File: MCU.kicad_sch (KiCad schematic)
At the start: 0 parts

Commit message: add power and processor and connectors
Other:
- note added: "Add programming connectors in this sheet"
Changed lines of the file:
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@@
 (kicad_sch (version 20211123) (generator eeschema)
   (paper "A4")
+  (text "Add programming connectors in this sheet \n" (at 17.78 19.05 0)
+    (effects (font (size 0.762 0.762)) (justify left bottom))
+  )
 )

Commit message: MCU added
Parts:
- added ?: STM32H725ZGT6, symbol STM32H725ZGT6:STM32H725ZGT6
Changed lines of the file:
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@@
     (effects (font (size 0.762 0.762)) (justify left bottom))
   )
+  (symbol (lib_id "STM32H725ZGT6:STM32H725ZGT6") (at 80.645 46.99 0) (unit 1)
+    (in_bom yes) (on_board yes) (fields_autoplaced)
+    (property "Reference" "?" (id 0) (at 189.23 35.3312 0))
+    (property "Value" "STM32H725ZGT6" (id 1) (at 189.23 37.8712 0))
+    (property "Footprint" "" (id 2) (at 80.645 46.99 0)
+      (effects (font (size 1.27 1.27)) hide)
+    )
+    (property "Datasheet" "" (id 3) (at 80.645 46.99 0)
+      (effects (font (size 1.27 1.27)) hide)
+    )
+    (property "Reference_1" "IC" (id 4) (at 189.23 40.4112 0))
+    (property "Value_1" "STM32H725ZGT6" (id 5) (at 189.23 42.9512 0))
+    (property "Footprint_1" "QFP50P2200X2200X160-144N" (id 6) (at 180.975 129.21 0)
+      (effects (font (size 1.27 1.27)) (justify left top) hide)
+    )
+    (property "Datasheet_1" "https://www.st.com/resource/en/datasheet/stm32h725ag.pdf" (id 7) (at 180.975 229.21 0)
+      (effects (font (size 1.27 1.27)) (justify left top) hide)
+    )
+    (property "Height" "1.6" (id 8) (at 180.975 429.21 0)
+      (effects (font (size 1.27 1.27)) (justify left top) hide)
+    )
+    (property "Mouser Part Number" "511-STM32H725ZGT6" (id 9) (at 180.975 529.21 0)
+      (effects (font (size 1.27 1.27)) (justify left top) hide)
+    )
+    (property "Mouser Price/Stock" "https://www.mouser.co.uk/ProductDetail/STMicroelectronics/STM32H725ZGT6?qs=sPbYRqrBIVkxUSEHgllpOw%3D%3D" (id 10) (at 180.975 629.21 0)
+      (effects (font (size 1.27 1.27)) (justify left top) hide)
+    )
+    (property "Manufacturer_Name" "STMicroelectronics" (id 11) (at 180.975 729.21 0)
+      (effects (font (size 1.27 1.27)) (justify left top) hide)
+    )
+    (property "Manufacturer_Part_Number" "STM32H725ZGT6" (id 12) (at 180.975 829.21 0)
+      (effects (font (size 1.27 1.27)) (justify left top) hide)
+    )
+    (pin "1")
+    (pin "10")
+    (pin "100")
+    (pin "101")
+    (pin "102")
+    (pin "103")
+    (pin "104")
+    (pin "105")
+    (pin "106")
+    (pin "107")
+    (pin "108")
+    (pin "109")
+    (pin "11")
+    (pin "110")
+    (pin "111")
+    (pin "112")
+    (pin "113")
+    (pin "114")
+    (pin "115")
+    (pin "116")
+    (pin "117")
+    (pin "118")
+    (pin "119")
+    (pin "12")
+    (pin "120")
+    (pin "121")
+    (pin "122")
+    (pin "123")
+    (pin "124")
+    (pin "125")
+    (pin "126")
+    (pin "127")
+    (pin "128")
+    (pin "129")
+    (pin "13")
+    (pin "130")
+    (pin "131")
+    (pin "132")
+    (pin "133")
+    (pin "134")
+    (pin "135")
+    (pin "136")
+    (pin "137")
+    (pin "138")
+    (pin "139")
+    (pin "14")
+    (pin "140")
+    (pin "141")
+    (pin "142")
+    (pin "143")
+    (pin "144")
+    (pin "15")
+    (pin "16")
+    (pin "17")
+    (pin "18")
+    (pin "19")
+    (pin "2")
+    (pin "20")
+    (pin "21")
+    (pin "22")
+    (pin "23")
+    (pin "24")
+    (pin "25")
+    (pin "26")
+    (pin "27")
+    (pin "28")
+    (pin "29")
+    (pin "3")
+    (pin "30")
+    (pin "31")
+    (pin "32")
+    (pin "33")
+    (pin "34")
+    (pin "35")
+    (pin "36")
+    (pin "37")
+    (pin "38")
+    (pin "39")
+    (pin "4")
+    (pin "40")
+    (pin "41")
+    (pin "42")
+    (pin "43")
+    (pin "44")
+    (pin "45")
+    (pin "46")
+    (pin "47")
+    (pin "48")
+    (pin "49")
+    (pin "5")
+    (pin "50")
+    (pin "51")
+    (pin "52")
+    (pin "53")
+    (pin "54")
+    (pin "55")
+    (pin "56")
+    (pin "57")
+    (pin "58")
+    (pin "59")
+    (pin "6")
+    (pin "60")
+    (pin "61")
+    (pin "62")
+    (pin "63")
+    (pin "64")
+    (pin "65")
+    (pin "66")
+    (pin "67")
+    (pin "68")
+    (pin "69")
+    (pin "7")
+    (pin "70")
+    (pin "71")
+    (pin "72")
+    (pin "73")
+    (pin "74")
+    (pin "75")
+    (pin "76")
+    (pin "77")
+    (pin "78")
+    (pin "79")
+    (pin "8")
+    (pin "80")
+    (pin "81")
+    (pin "82")
+    (pin "83")
+    (pin "84")
+    (pin "85")
+    (pin "86")
+    (pin "87")
+    (pin "88")
+    (pin "89")
+    (pin "9")
+    (pin "90")
+    (pin "91")
+    (pin "92")
+    (pin "93")
+    (pin "94")
+    (pin "95")
+    (pin "96")
+    (pin "97")
+    (pin "98")
+    (pin "99")
+  )
 )

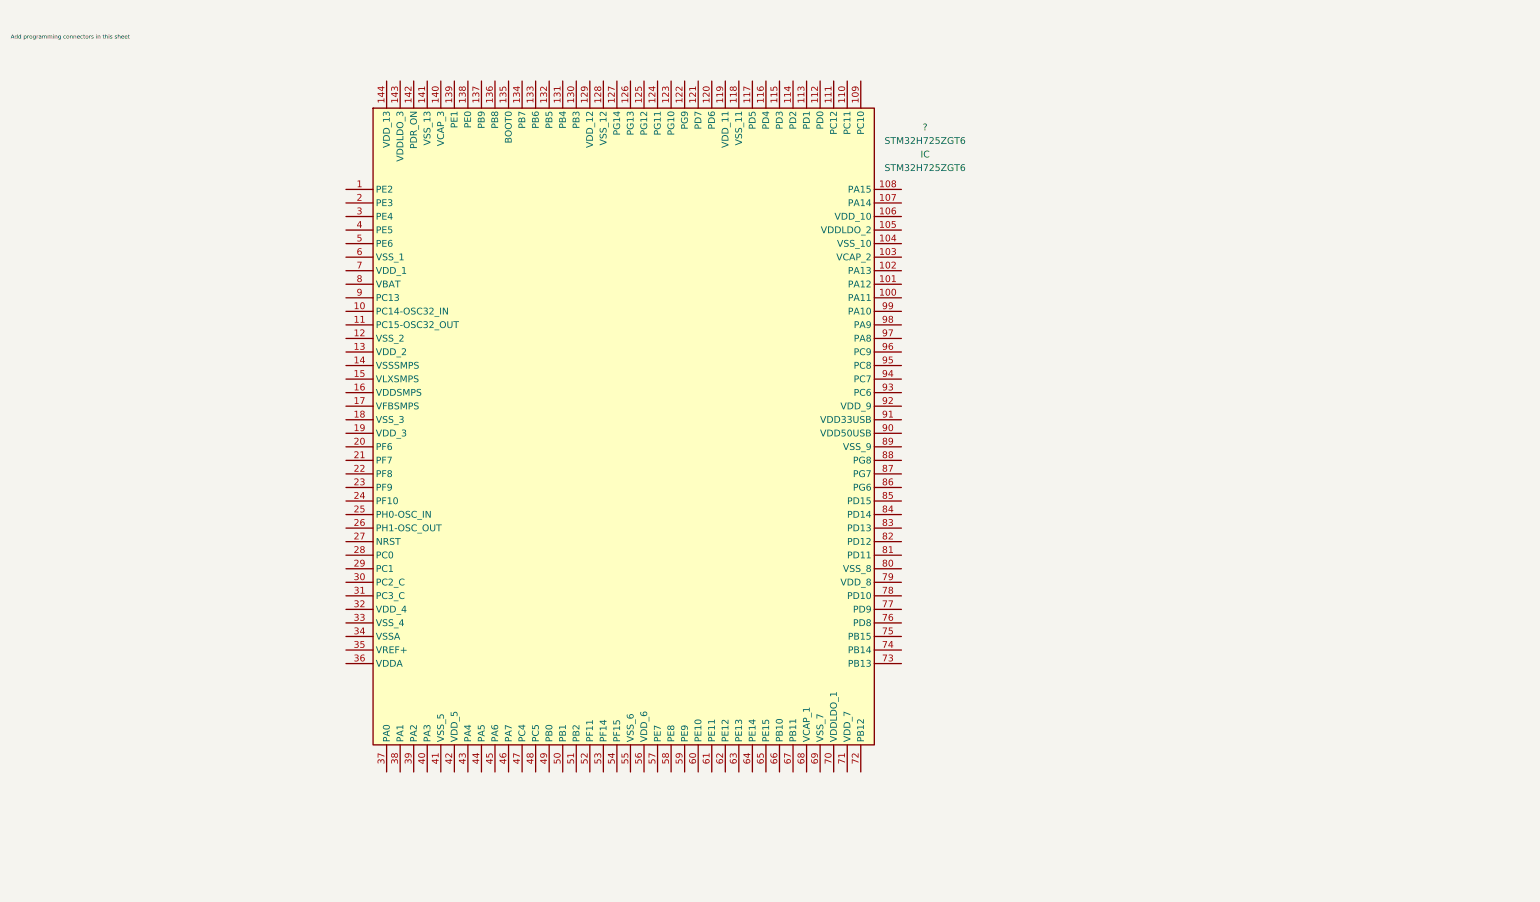
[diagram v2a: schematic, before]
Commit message: MCU_pinout_except_timer please add connector symbols and footprint folder, i will send you parts throughout the day
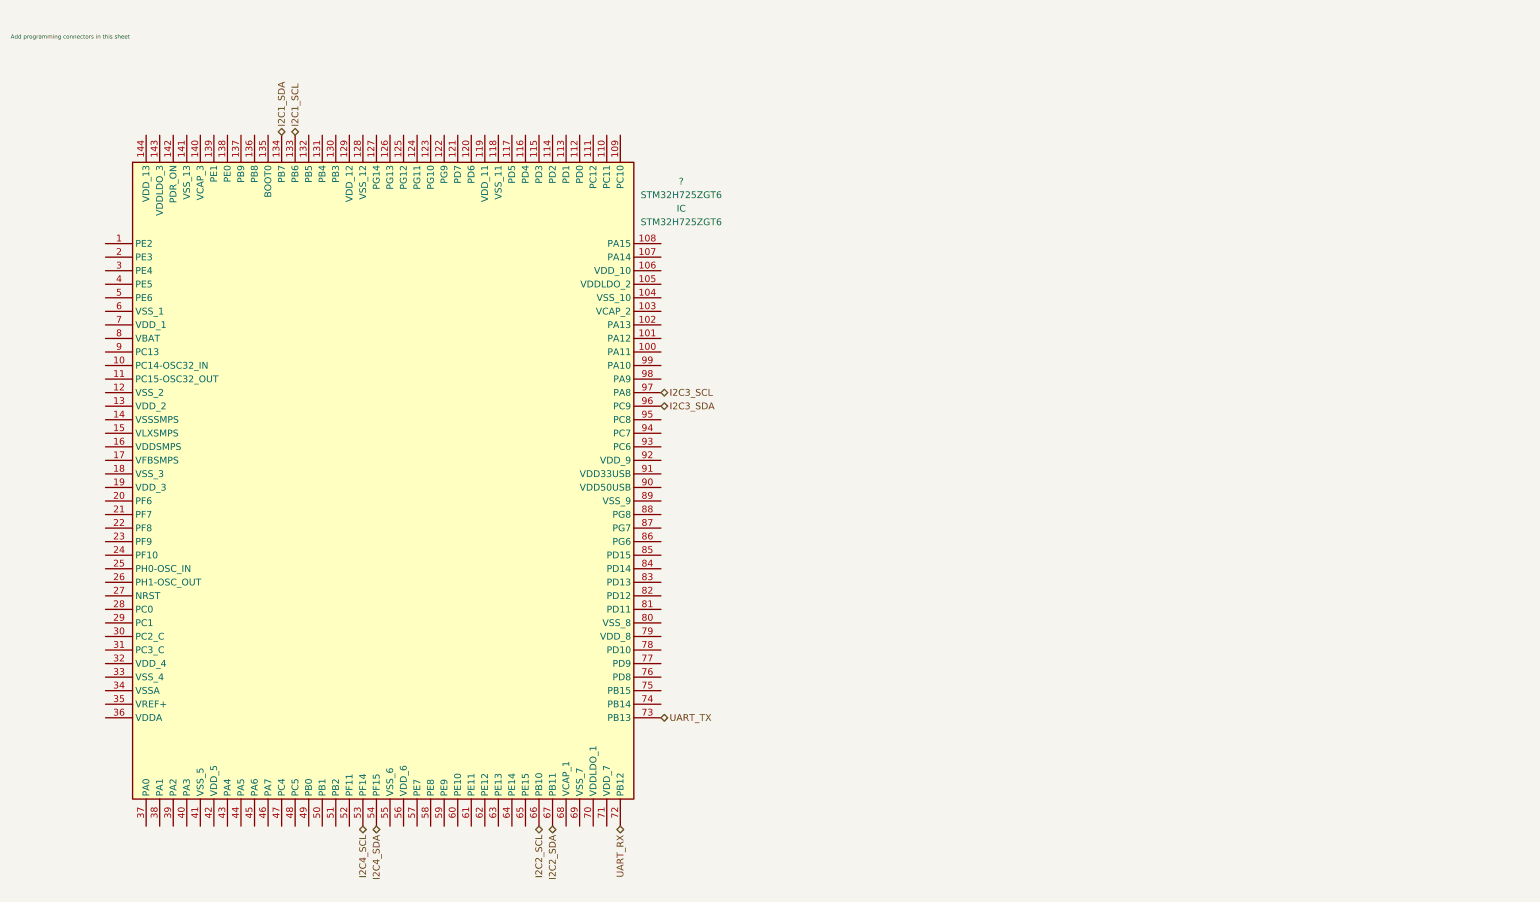
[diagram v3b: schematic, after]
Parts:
- removed ?: STM32H725ZGT6, symbol STM32H725ZGT6:STM32H725ZGT6
- added ?: STM32H725ZGT6, symbol STM32H725ZGT6:STM32H725ZGT6
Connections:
- new net I2C1_SCL: ?.133 (PB6)
- new net I2C1_SDA: ?.134 (PB7)
- new net I2C2_SCL: ?.66 (PB10)
- new net I2C2_SDA: ?.67 (PB11)
- new net I2C3_SCL: ?.97 (PA8)
- new net I2C3_SDA: ?.96 (PC9)
- new net I2C4_SCL: ?.53 (PF14)
- new net I2C4_SDA: ?.54 (PF15)
- new net UART_RX: ?.72 (PB12)
- new net UART_TX: ?.73 (PB13)
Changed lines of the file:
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@@
     (effects (font (size 0.762 0.762)) (justify left bottom))
   )
-  (symbol (lib_id "STM32H725ZGT6:STM32H725ZGT6") (at 80.645 46.99 0) (unit 1)
+  (hierarchical_label "I2C4_SDA" (shape bidirectional) (at 86.36 166.37 270)
+    (effects (font (size 1.27 1.27)) (justify right))
+  )
+  (hierarchical_label "I2C2_SCL" (shape bidirectional) (at 116.84 166.37 270)
+    (effects (font (size 1.27 1.27)) (justify right))
+  )
+  (hierarchical_label "I2C4_SCL" (shape bidirectional) (at 83.82 166.37 270)
+    (effects (font (size 1.27 1.27)) (justify right))
+  )
+  (hierarchical_label "UART_RX" (shape bidirectional) (at 132.08 166.37 270)
+    (effects (font (size 1.27 1.27)) (justify right))
+  )
+  (hierarchical_label "I2C2_SDA" (shape bidirectional) (at 119.38 166.37 270)
+    (effects (font (size 1.27 1.27)) (justify right))
+  )
+  (hierarchical_label "UART_TX" (shape bidirectional) (at 139.7 146.05 0)
+    (effects (font (size 1.27 1.27)) (justify left))
+  )
+  (hierarchical_label "I2C1_SCL" (shape bidirectional) (at 71.12 36.83 90)
+    (effects (font (size 1.27 1.27)) (justify left))
+  )
+  (hierarchical_label "I2C3_SCL" (shape bidirectional) (at 139.7 85.09 0)
+    (effects (font (size 1.27 1.27)) (justify left))
+  )
+  (hierarchical_label "I2C1_SDA" (shape bidirectional) (at 68.58 36.83 90)
+    (effects (font (size 1.27 1.27)) (justify left))
+  )
+  (hierarchical_label "I2C3_SDA" (shape bidirectional) (at 139.7 87.63 0)
+    (effects (font (size 1.27 1.27)) (justify left))
+  )
+  (symbol (lib_id "STM32H725ZGT6:STM32H725ZGT6") (at 35.56 57.15 0) (unit 1)
     (in_bom yes) (on_board yes) (fields_autoplaced)
-    (property "Reference" "?" (id 0) (at 189.23 35.3312 0))
-    (property "Value" "STM32H725ZGT6" (id 1) (at 189.23 37.8712 0))
-    (property "Footprint" "" (id 2) (at 80.645 46.99 0)
+    (property "Reference" "?" (id 0) (at 143.51 45.4912 0))
+    (property "Value" "STM32H725ZGT6" (id 1) (at 143.51 48.0312 0))
+    (property "Footprint" "" (id 2) (at 35.56 57.15 0)
       (effects (font (size 1.27 1.27)) hide)
     )
-    (property "Datasheet" "" (id 3) (at 80.645 46.99 0)
+    (property "Datasheet" "" (id 3) (at 35.56 57.15 0)
       (effects (font (size 1.27 1.27)) hide)
     )
-    (property "Reference_1" "IC" (id 4) (at 189.23 40.4112 0))
-    (property "Value_1" "STM32H725ZGT6" (id 5) (at 189.23 42.9512 0))
-    (property "Footprint_1" "QFP50P2200X2200X160-144N" (id 6) (at 180.975 129.21 0)
+    (property "Reference_1" "IC" (id 4) (at 143.51 50.5712 0))
+    (property "Value_1" "STM32H725ZGT6" (id 5) (at 143.51 53.1112 0))
+    (property "Footprint_1" "QFP50P2200X2200X160-144N" (id 6) (at 135.89 139.37 0)
       (effects (font (size 1.27 1.27)) (justify left top) hide)
     )
-    (property "Datasheet_1" "https://www.st.com/resource/en/datasheet/stm32h725ag.pdf" (id 7) (at 180.975 229.21 0)
+    (property "Datasheet_1" "https://www.st.com/resource/en/datasheet/stm32h725ag.pdf" (id 7) (at 135.89 239.37 0)
       (effects (font (size 1.27 1.27)) (justify left top) hide)
     )
-    (property "Height" "1.6" (id 8) (at 180.975 429.21 0)
+    (property "Height" "1.6" (id 8) (at 135.89 439.37 0)
       (effects (font (size 1.27 1.27)) (justify left top) hide)
     )
-    (property "Mouser Part Number" "511-STM32H725ZGT6" (id 9) (at 180.975 529.21 0)
+    (property "Mouser Part Number" "511-STM32H725ZGT6" (id 9) (at 135.89 539.37 0)
       (effects (font (size 1.27 1.27)) (justify left top) hide)
     )
-    (property "Mouser Price/Stock" "https://www.mouser.co.uk/ProductDetail/STMicroelectronics/STM32H725ZGT6?qs=sPbYRqrBIVkxUSEHgllpOw%3D%3D" (id 10) (at 180.975 629.21 0)
+    (property "Mouser Price/Stock" "https://www.mouser.co.uk/ProductDetail/STMicroelectronics/STM32H725ZGT6?qs=sPbYRqrBIVkxUSEHgllpOw%3D%3D" (id 10) (at 135.89 639.37 0)
       (effects (font (size 1.27 1.27)) (justify left top) hide)
     )
-    (property "Manufacturer_Name" "STMicroelectronics" (id 11) (at 180.975 729.21 0)
+    (property "Manufacturer_Name" "STMicroelectronics" (id 11) (at 135.89 739.37 0)
       (effects (font (size 1.27 1.27)) (justify left top) hide)
     )
-    (property "Manufacturer_Part_Number" "STM32H725ZGT6" (id 12) (at 180.975 829.21 0)
+    (property "Manufacturer_Part_Number" "STM32H725ZGT6" (id 12) (at 135.89 839.37 0)
       (effects (font (size 1.27 1.27)) (justify left top) hide)
     )

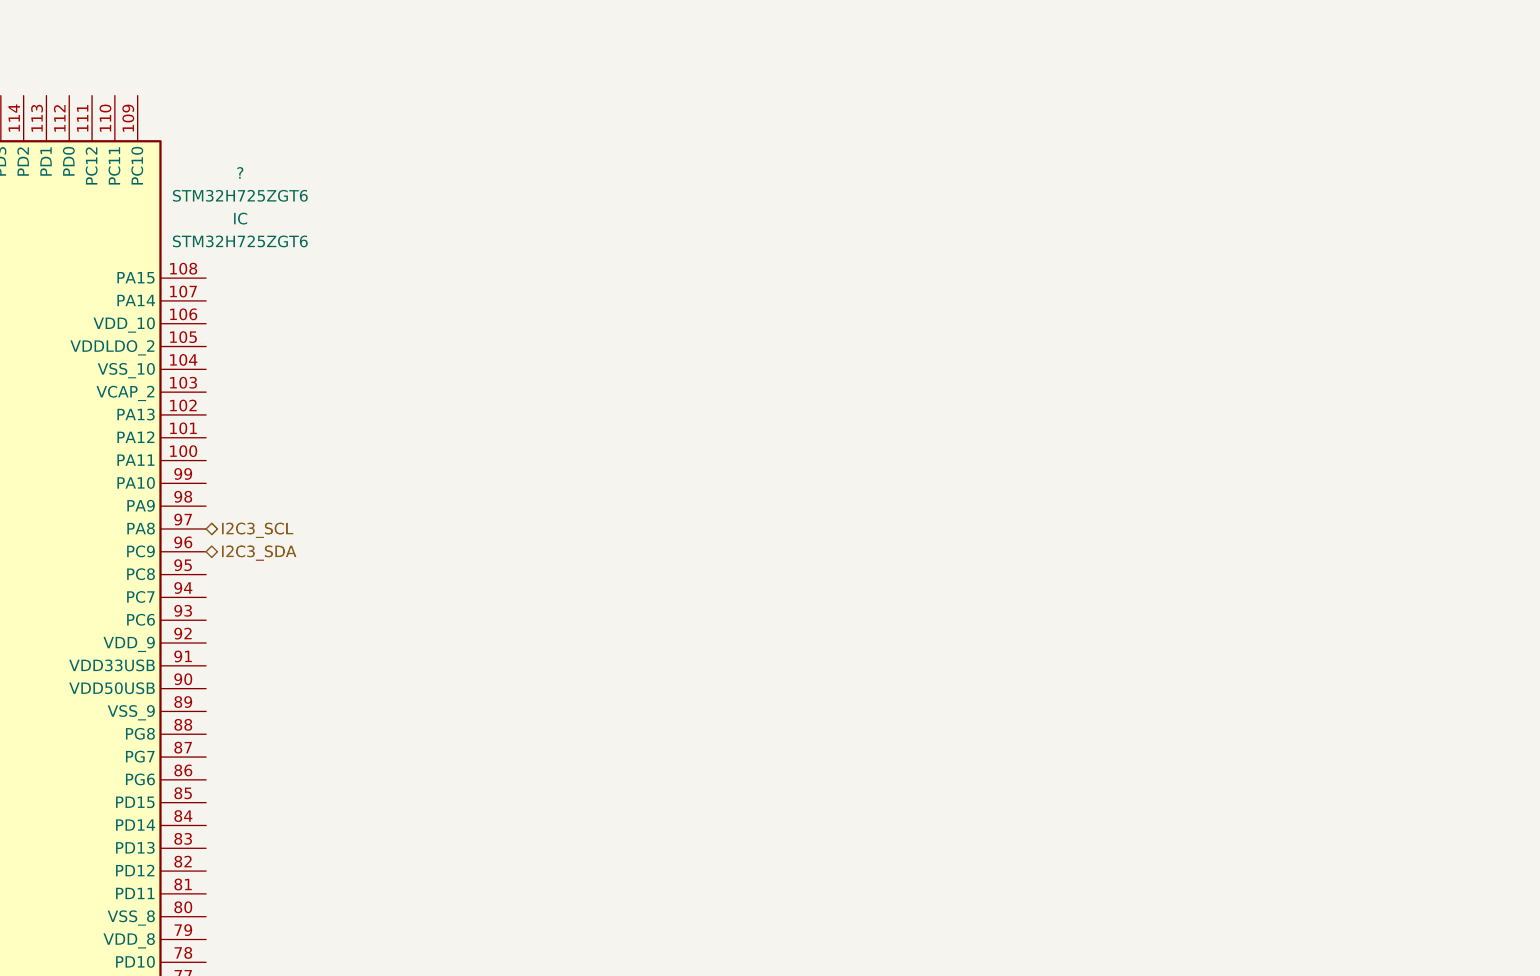
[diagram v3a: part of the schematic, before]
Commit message: Motor symbol corrected, Oscillator circuitry added and external footprints added
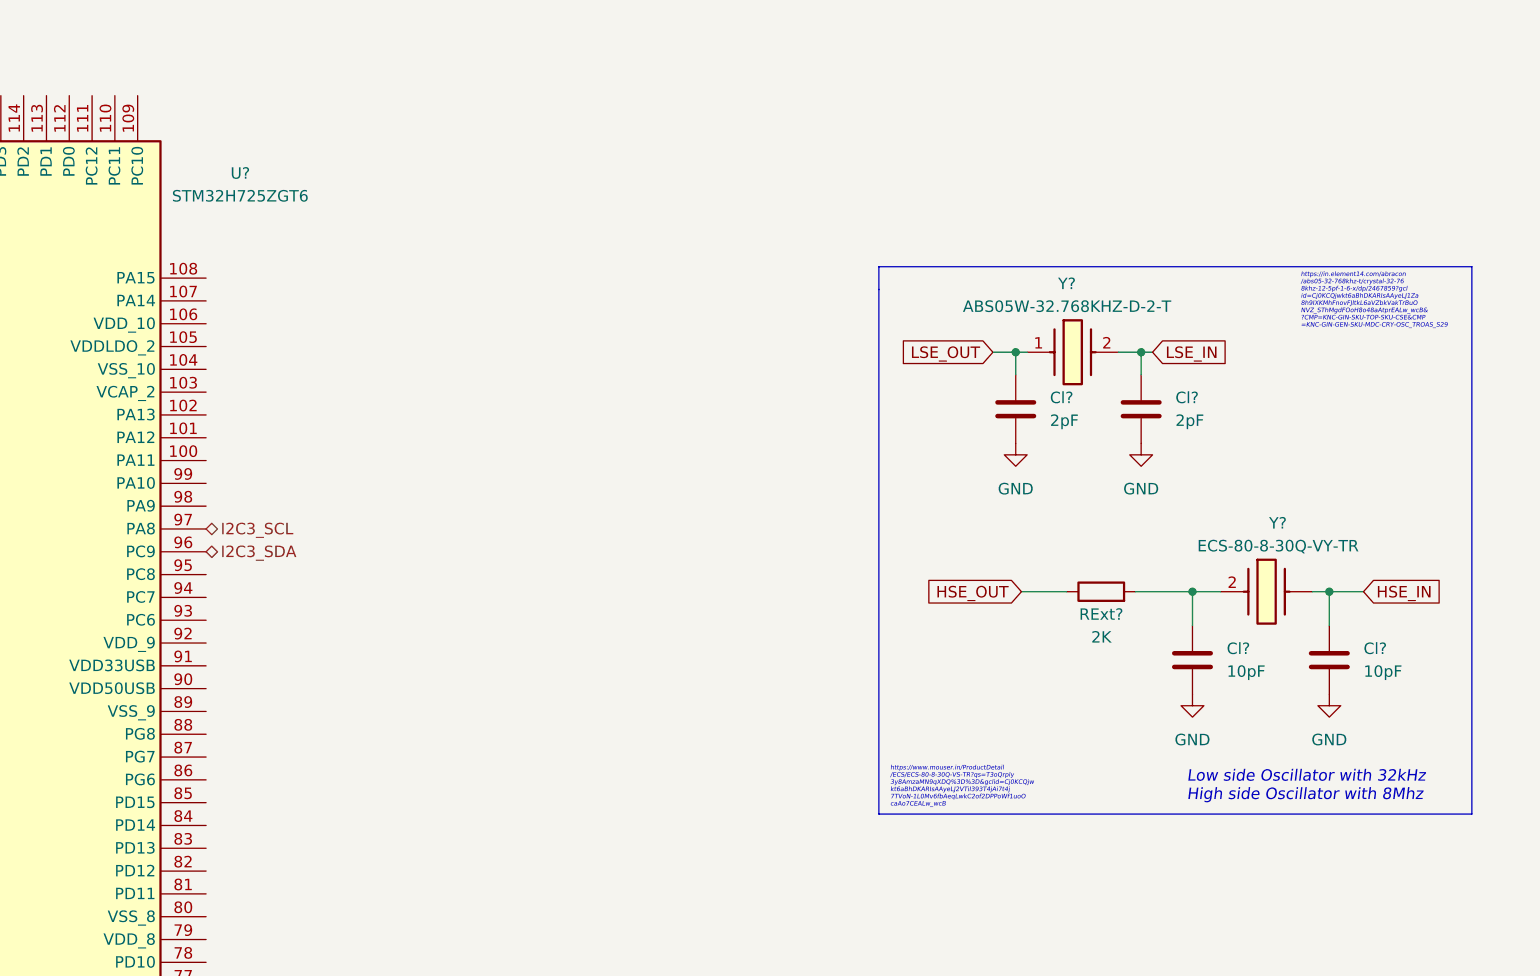
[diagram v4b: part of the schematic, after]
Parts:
- added Cl? (x2): 10pF, Capacitor_SMD:C_0402_1005Metric, symbol Device:C
- added Cl? (x2): 2pF, Capacitor_SMD:C_0402_1005Metric, symbol Device:C
- added RExt?: 2K, Resistor_SMD:R_0603_1608Metric, symbol Device:R
- added Y?: ABS05W-32.768KHZ-D-2-T, ABS05W-32.768KHZ-D-2-T:ABS05W32768KHZD2T, symbol ABS05W-32_768KHZ-D-2-T:ABS05W-32.768KHZ-D-2-T
- added Y?: ECS-80-8-30Q-VY-TR, ECS-80-8-30Q-VY-TR:ECS80830QVYTR, symbol ECS-80-8-30Q-VY-TR:ECS-80-8-30Q-VY-TR
- U?: renamed from ?; footprint (none) -> STM32H725ZGT6:QFP50P2200X2200X160-144N; now left out of the parts list
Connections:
- new net: Cl?.1, RExt?.2, Y?.2 (CRYSTAL_2)
- new net GND: Cl?.2, Cl?.2, Cl?.2, Cl?.2
- new net HSE_IN: Cl?.1, Y?.
- new net HSE_OUT: RExt?.1
- new net LSE_IN: Cl?.1, Y?.2
- new net LSE_OUT: Cl?.1, Y?.1
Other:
- note added: "Low side Oscillator with 32kHz High side Oscillator with 8Mhz"
- note added: "https://in.element14.com/abracon /abs05-32-768khz-t/crystal-32-76 8khz-12-5pf-1-6-x/dp/2467859?gcl id=Cj0KCQjwkt6aBhDKARIsAAyeLJ1Za 8h9IXKMhFnovFJltkL6aVZbkVakTrBuO NVZ_SThMgdFOoH8o48aAtprEALw_wcB& ?CMP=KNC-GIN-SKU-TOP-SKU-CSE&CMP =KNC-GIN-GEN-SKU-MDC-CRY-OSC_TROAS_S29"
- note added: "https://www.mouser.in/ProductDetail /ECS/ECS-80-8-30Q-VS-TR?qs=T3oQrply 3y8AmzaMN9qXDQ%3D%3D&gclid=Cj0KCQjw kt6aBhDKARIsAAyeLJ2VTiI393T4jAi7t4j 7TVoN-1L0Mv6fbAeqLwkC2of2DPPoWf1uoO caAo7CEALw_wcB"
